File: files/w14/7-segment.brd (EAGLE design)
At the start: 100 x 80 mm, 21 parts, among them IC2 5V

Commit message: routing in progress
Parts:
- removed IC2: 5V, fab:SOT23
- removed U$2: PINHD-2X2-SMD, fab:2X02SMD
- moved RA 45.0 mm to (44.5, 76.2), turned to 0 degrees
- moved RF 36.4 mm to (29.2, 72.4), turned to 90 degrees
- moved RB 31.9 mm to (39.4, 66.0), turned to 180 degrees
- moved RG 31.5 mm to (39.4, 57.1), turned to 180 degrees
- moved U$3 29.5 mm to (41.9, 3.81), turned to 270 degrees
- moved C1 28.5 mm to (41.9, 8.89), turned to 180 degrees
- moved U$1 25.6 mm to (40.6, 28.6)
- moved R16 23.6 mm to (41.9, 12.1)
- moved RE 22.9 mm to (29.2, 59.7), turned to 0 degrees
- moved RC 15.5 mm to (41.9, 52.1), turned to 180 degrees
- moved RD 12.0 mm to (44.5, 45.7), turned to 0 degrees
- moved U$17 8.25 mm to (41.9, 18.4), turned to 90 degrees
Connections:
- removed net VIN: IC2.2, U$2.2
- net GND: now also U$3.1; no longer IC2.3, U$2.4
- net VCC: now also U$3.3; no longer IC2.1
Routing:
- net SCK: track 0.00 -> 75.3 mm, vias 0 -> 2
- net MOSI: track 0.38 -> 73.1 mm
- net PB4: track 0.00 -> 52.2 mm
- net MISO: track 0.00 -> 41.9 mm
- net GND: track 0.00 -> 24.4 mm
- net N$7: track 0.00 -> 11.7 mm
- net N$4: track 0.00 -> 8.67 mm
- net N$5: track 0.00 -> 6.13 mm
- net RST: track 0.00 -> 5.07 mm
- net N$11: track 0.00 -> 3.81 mm
- net N$8: track 0.00 -> 1.78 mm
- net N$2: track 0.00 -> 1.78 mm

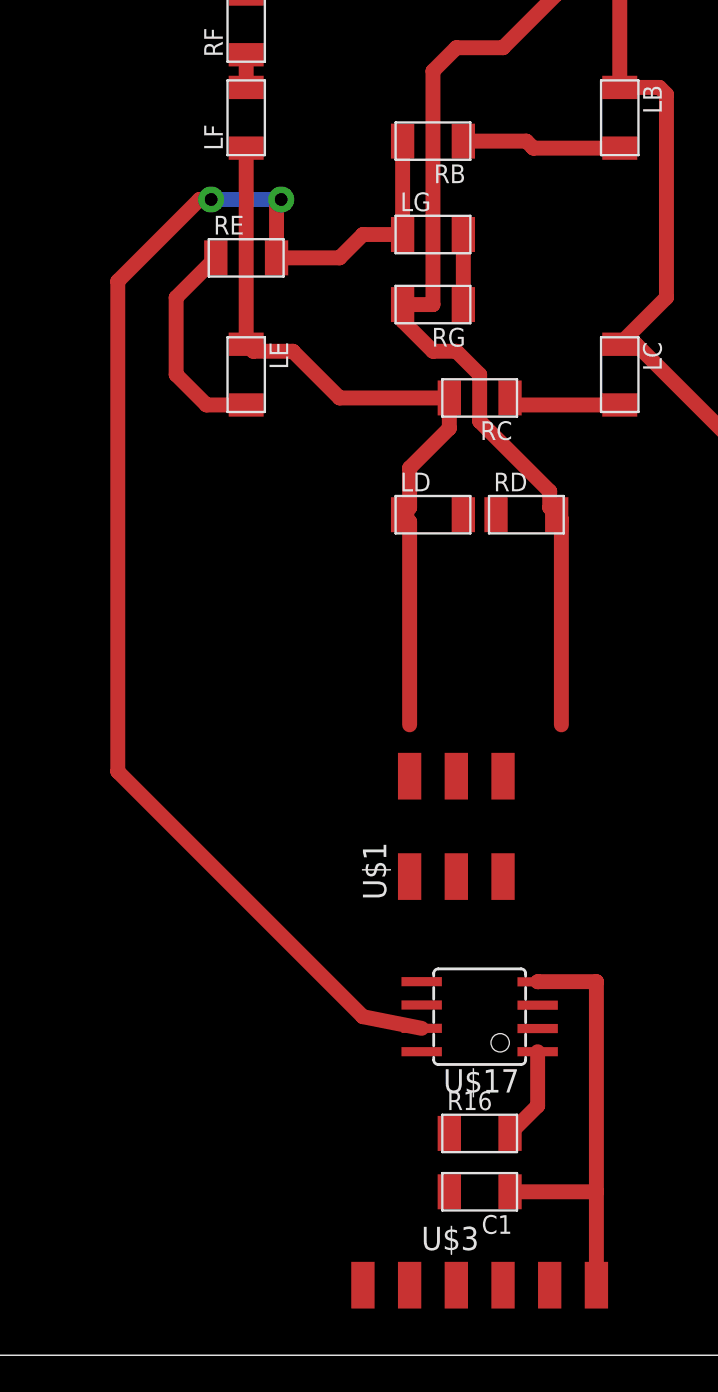
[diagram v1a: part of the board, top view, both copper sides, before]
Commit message: schematic without ISP header done
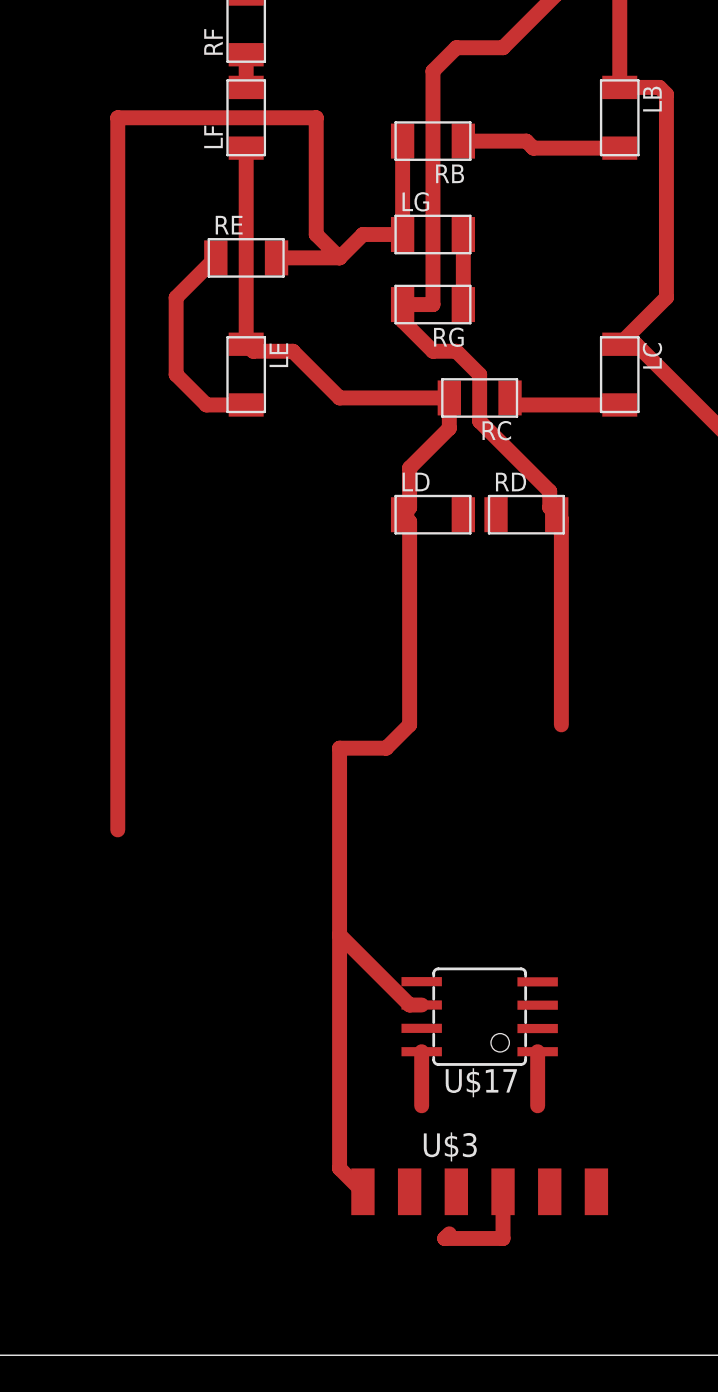
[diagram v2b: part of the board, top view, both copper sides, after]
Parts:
- removed C1: (no value), fab:C1206FAB
- removed R16: (no value), fab:R1206FAB
- removed U$1: AVRISPSMD, fab:2X03SMD
- moved U$3 5.08 mm to (41.9, 8.89)
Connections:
- removed net RX: U$17.2, U$3.5
- new net PB3: LG.1, RB.2, RE.2, U$17.2
- net GND: no longer C1.1, U$1.6
- net MISO: now also U$3.6; no longer U$1.1
- net MOSI: now also U$3.5; no longer LA.1, LB.1, LC.1, RF.2, U$1.4
- net RST: now also U$3.2; no longer R16.2, U$1.5
- net SCK: now also LA.1, LB.1, LC.1, RF.2, U$3.4; no longer LG.1, RB.2, RE.2, U$1.3
- net VCC: no longer C1.2, R16.1, U$1.2
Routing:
- net MOSI: track 73.1 -> 0.00 mm
- net PB3: track 0.00 -> 70.1 mm
- net MISO: track 41.9 -> 77.0 mm
- net GND: track 24.4 -> 0.00 mm
- net VCC: track 0.00 -> 9.02 mm
- net SCK: track 75.3 -> 73.1 mm, vias 2 -> 0
- net RST: track 5.07 -> 2.94 mm

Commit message: board programmed
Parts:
- added R1: 0, fab:R1206FAB
- moved LB 29.7 mm to (27.4, 47.5)
- moved LC 29.7 mm to (27.4, 33.5)
- moved RA 29.7 mm to (22.4, 56.4)
- moved LA 29.7 mm to (17.3, 56.4)
- moved LE 29.7 mm to (7.11, 33.5)
- moved LF 29.7 mm to (7.11, 47.5)
- moved RB 29.7 mm to (17.3, 46.2)
- moved RD 29.7 mm to (22.4, 25.9)
- moved LD 29.7 mm to (17.3, 25.9)
- moved LG 29.7 mm to (17.3, 41.1)
- moved RC 29.7 mm to (19.8, 32.3)
- moved RE 29.7 mm to (7.11, 39.9)
- moved RF 29.7 mm to (7.11, 52.6)
- moved RG 29.7 mm to (17.3, 37.3)
- moved U$17 25.1 mm to (17.3, 13.8)
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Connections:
- net MISO: now also U$3.5; no longer LD.1, LE.1, LF.1, RC.2, U$3.6
- net MOSI: now also LD.1, LE.1, LF.1, RC.2, U$3.6; no longer U$3.5
- net PB3: now also R1.1, R1.2
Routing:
- net MOSI: track 0.00 -> 61.8 mm
- net MISO: track 77.0 -> 16.9 mm
- net SCK: track 73.1 -> 122.8 mm
- net GND: track 0.00 -> 14.6 mm
- net PB4: track 52.2 -> 61.3 mm
- net PB3: track 70.1 -> 78.5 mm
- net RST: track 2.94 -> 8.28 mm
- net N$6: track 0.00 -> 1.78 mm
- net VCC: track 9.02 -> 10.6 mm
- net N$7: track 11.7 -> 11.0 mm
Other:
- board size 100 x 80 mm -> 32.4 x 62.1 mm
